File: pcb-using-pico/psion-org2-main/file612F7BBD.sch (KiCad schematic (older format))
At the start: 36 parts, among them SW1 AC_ON, SW10 n, SW11 t, SW12 del, SW13 up, SW14 c, SW15 i, SW16 o, SW17 u, SW18 y, SW19 down, SW2 A, SW20 d, SW21 j, SW22 p, SW23 v, SW24 z, SW25 left, SW26 e, SW27 k, SW28 q, SW29 w, SW3 g, SW30 spc, SW31 right, SW32 f, SW33 L, SW34 r, SW35 x, SW36 exe, SW4 m, SW5 s, SW6 shft, SW7 mode, SW8 b, SW9 h

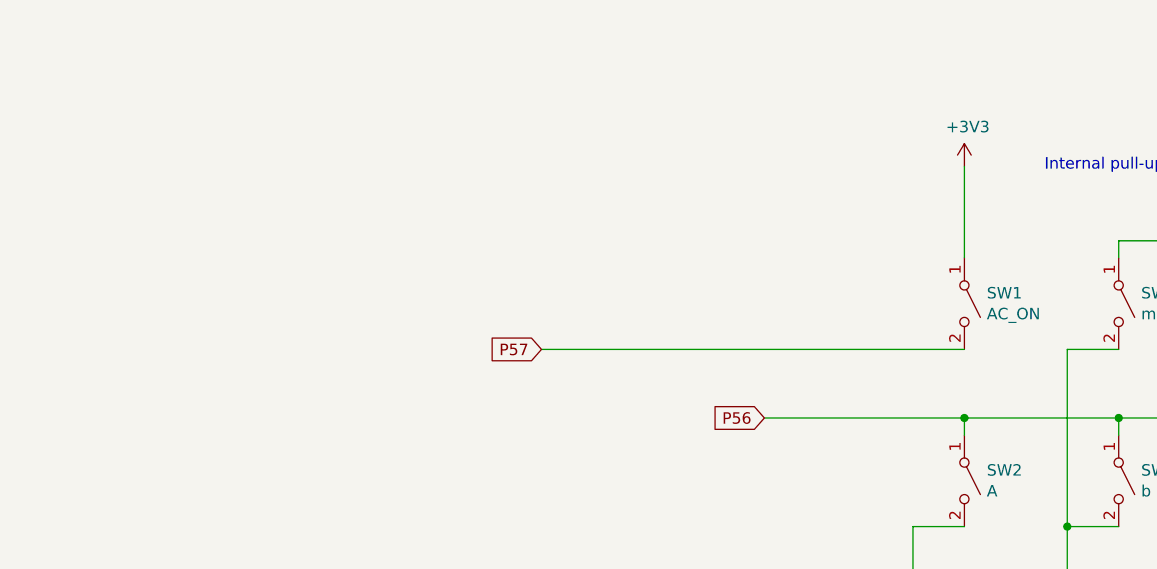
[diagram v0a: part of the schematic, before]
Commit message: Added second connector, eeprom on power pcb
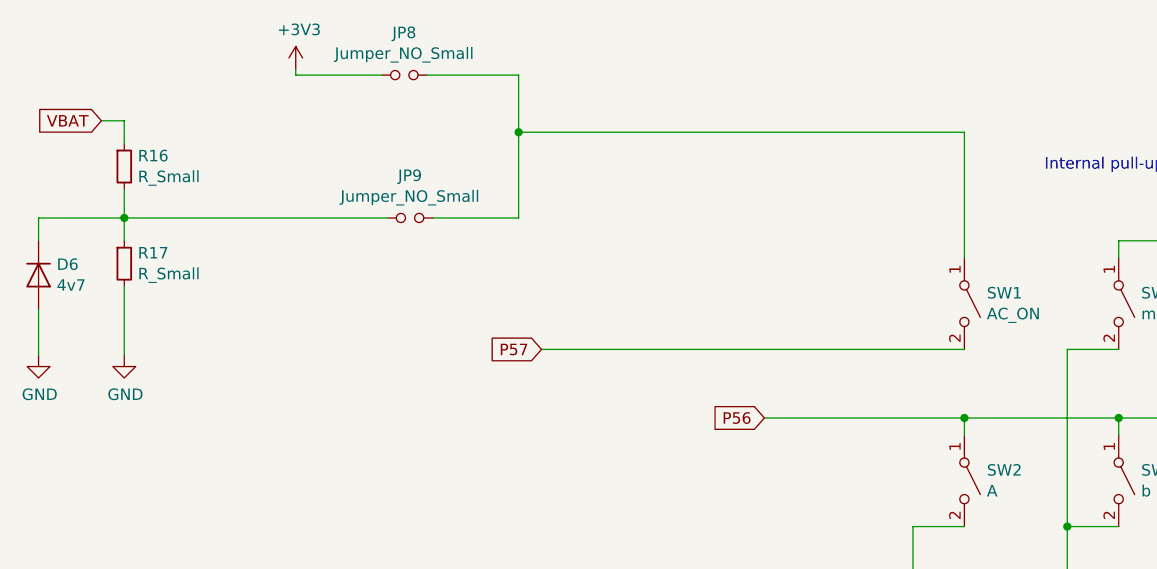
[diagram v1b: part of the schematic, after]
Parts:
- added D6: 4v7, Diode_SMD:D_SOD-123, symbol Device:D
- added JP8, JP9: Jumper_NO_Small, Jumper:SolderJumper-2_P1.3mm_Open_RoundedPad1.0x1.5mm, symbol Device:Jumper_NO_Small
- added R16, R17: R_Small, Resistor_SMD:R_0805_2012Metric, symbol Device:R_Small
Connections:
- net +3V3: now also JP8.1; no longer SW1.1 (A)
- new net: JP8.2, JP9.2, SW1.1 (A)
- new net: D6.1 (K), JP9.1, R16.2, R17.1
- new net GND: D6.2 (A), R17.2
- new net VBAT: R16.1
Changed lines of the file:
@@
 L power:+3V3 #PWR036
 U 1 1 61827F51
-P 6050 1150
-F 0 "#PWR036" H 6050 1000 50  0001 C CNN
-F 1 "+3V3" H 6065 1323 50  0000 C CNN
-F 2 "" H 6050 1150 50  0001 C CNN
-F 3 "" H 6050 1150 50  0001 C CNN
-	1    6050 1150
+P 3125 725
+F 0 "#PWR036" H 3125 575 50  0001 C CNN
+F 1 "+3V3" H 3140 898 50  0000 C CNN
+F 2 "" H 3125 725 50  0001 C CNN
+F 3 "" H 3125 725 50  0001 C CNN
+	1    3125 725
 	1    0    0    -1
 $EndComp
-Wire Wire Line
-	6050 1150 6050 1550
 Text GLabel 9875 950  1    50   Input ~ 0
 K1
@@
 Wire Wire Line
 	5200 5175 6050 5175
+$Comp
+L Device:R_Small R17
+U 1 1 618E7FEC
+P 2375 1575
+F 0 "R17" H 2434 1621 50  0000 L CNN
+F 1 "R_Small" H 2434 1530 50  0000 L CNN
+F 2 "Resistor_SMD:R_0805_2012Metric" H 2375 1575 50  0001 C CNN
+F 3 "~" H 2375 1575 50  0001 C CNN
+	1    2375 1575
+	1    0    0    -1
+$EndComp
+$Comp
+L Device:R_Small R16
+U 1 1 618E840C
+P 2375 1150
+F 0 "R16" H 2434 1196 50  0000 L CNN
+F 1 "R_Small" H 2434 1105 50  0000 L CNN
+F 2 "Resistor_SMD:R_0805_2012Metric" H 2375 1150 50  0001 C CNN
+F 3 "~" H 2375 1150 50  0001 C CNN
+	1    2375 1150
+	1    0    0    -1
+$EndComp
+$Comp
+L Device:D D6
+U 1 1 618E8BE1
+P 2000 1625
+F 0 "D6" V 1954 1704 50  0000 L CNN
+F 1 "4v7" V 2045 1704 50  0000 L CNN
+F 2 "Diode_SMD:D_SOD-123" H 2000 1625 50  0001 C CNN
+F 3 "~" H 2000 1625 50  0001 C CNN
+	1    2000 1625
+	0    1    1    0
+$EndComp
+Wire Wire Line
+	3125 725  3125 750
+Wire Wire Line
+	6050 1000 6050 1550
+Wire Wire Line
+	2375 1050 2375 950
+Wire Wire Line
+	2375 1250 2375 1375
+Wire Wire Line
+	2375 1375 2000 1375
+Wire Wire Line
+	2000 1375 2000 1475
+Connection ~ 2375 1375
+Wire Wire Line
+	2375 1375 2375 1475
+$Comp
+L power:GND #PWR0110
+U 1 1 61919262
+P 2000 1975
+F 0 "#PWR0110" H 2000 1725 50  0001 C CNN
+F 1 "GND" H 2005 1802 50  0000 C CNN
+F 2 "" H 2000 1975 50  0001 C CNN
+F 3 "" H 2000 1975 50  0001 C CNN
+	1    2000 1975
+	1    0    0    -1
+$EndComp
+$Comp
+L power:GND #PWR0111
+U 1 1 619195FD
+P 2375 1975
+F 0 "#PWR0111" H 2375 1725 50  0001 C CNN
+F 1 "GND" H 2380 1802 50  0000 C CNN
+F 2 "" H 2375 1975 50  0001 C CNN
+F 3 "" H 2375 1975 50  0001 C CNN
+	1    2375 1975
+	1    0    0    -1
+$EndComp
+Wire Wire Line
+	2375 1975 2375 1675
+Wire Wire Line
+	2000 1975 2000 1775
+Text GLabel 2275 950  0    50   Input ~ 0
+VBAT
+Wire Wire Line
+	2275 950  2375 950
+$Comp
+L Device:Jumper_NO_Small JP8
+U 1 1 61F117AF
+P 3600 750
+F 0 "JP8" H 3600 935 50  0000 C CNN
+F 1 "Jumper_NO_Small" H 3600 844 50  0000 C CNN
+F 2 "Jumper:SolderJumper-2_P1.3mm_Open_RoundedPad1.0x1.5mm" H 3600 750 50  0001 C CNN
+F 3 "~" H 3600 750 50  0001 C CNN
+	1    3600 750
+	1    0    0    -1
+$EndComp
+$Comp
+L Device:Jumper_NO_Small JP9
+U 1 1 61F123C6
+P 3625 1375
+F 0 "JP9" H 3625 1560 50  0000 C CNN
+F 1 "Jumper_NO_Small" H 3625 1469 50  0000 C CNN
+F 2 "Jumper:SolderJumper-2_P1.3mm_Open_RoundedPad1.0x1.5mm" H 3625 1375 50  0001 C CNN
+F 3 "~" H 3625 1375 50  0001 C CNN
+	1    3625 1375
+	1    0    0    -1
+$EndComp
+Wire Wire Line
+	2375 1375 3525 1375
+Wire Wire Line
+	3125 750  3500 750
+Wire Wire Line
+	3725 1375 4100 1375
+Wire Wire Line
+	4100 1375 4100 1000
+Wire Wire Line
+	4100 750  3700 750
+Wire Wire Line
+	6050 1000 4100 1000
+Connection ~ 4100 1000
+Wire Wire Line
+	4100 1000 4100 750
 $EndSCHEMATC

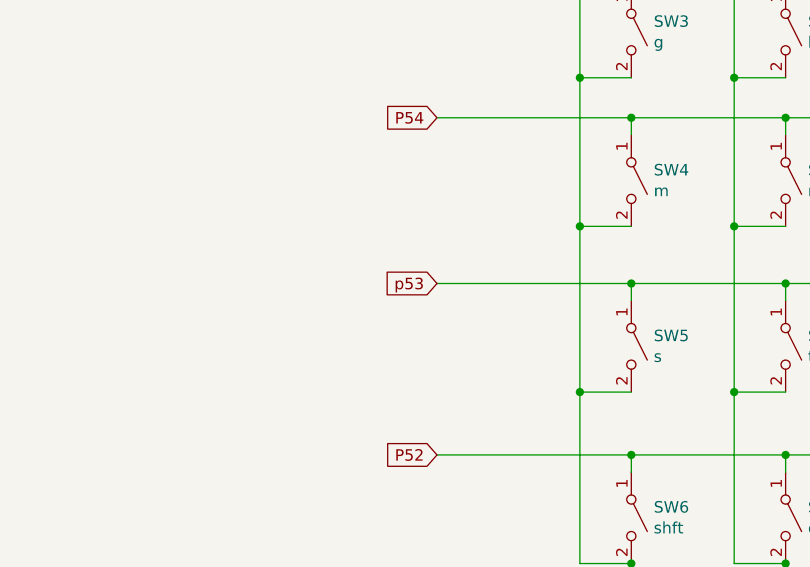
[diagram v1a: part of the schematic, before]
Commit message: Added fab1 archive and small fixes to emulator
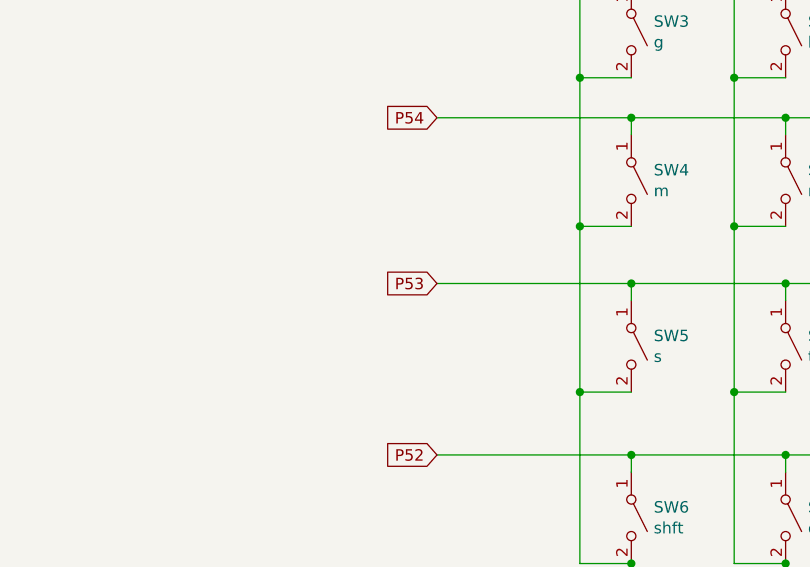
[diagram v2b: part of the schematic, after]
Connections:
- net p53 renamed P53
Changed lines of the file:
@@
 P54
 Text GLabel 5200 4425 0    50   Input ~ 0
-p53
+P53
 Text GLabel 5200 5175 0    50   Input ~ 0
 P52

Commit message: Updates after fab1
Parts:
- D6: value 4v7 -> 2v7
- R16: value R_Small -> 2k2
- R17: value R_Small -> nopop
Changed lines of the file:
@@
 P 2375 1575
 F 0 "R17" H 2434 1621 50  0000 L CNN
-F 1 "R_Small" H 2434 1530 50  0000 L CNN
+F 1 "nopop" H 2434 1530 50  0000 L CNN
 F 2 "Resistor_SMD:R_0805_2012Metric" H 2375 1575 50  0001 C CNN
 F 3 "~" H 2375 1575 50  0001 C CNN
@@
 P 2375 1150
 F 0 "R16" H 2434 1196 50  0000 L CNN
-F 1 "R_Small" H 2434 1105 50  0000 L CNN
+F 1 "2k2" H 2434 1105 50  0000 L CNN
 F 2 "Resistor_SMD:R_0805_2012Metric" H 2375 1150 50  0001 C CNN
 F 3 "~" H 2375 1150 50  0001 C CNN
@@
 P 2000 1625
 F 0 "D6" V 1954 1704 50  0000 L CNN
-F 1 "4v7" V 2045 1704 50  0000 L CNN
+F 1 "2v7" V 2045 1704 50  0000 L CNN
 F 2 "Diode_SMD:D_SOD-123" H 2000 1625 50  0001 C CNN
 F 3 "~" H 2000 1625 50  0001 C CNN

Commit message: V1.1 started
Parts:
- removed JP8, JP9: Jumper_NO_Small, Jumper:SolderJumper-2_P1.3mm_Open_RoundedPad1.0x1.5mm, symbol Device:Jumper_NO_Small
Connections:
- net K3: no longer SW7.2 (B)
- net K4: no longer SW13.2 (B)
- net K5: no longer SW25.2 (B)
- net K6: no longer SW31.2 (B)
- net K7: no longer SW19.2 (B)
- net P52: now also SW7.2 (B)
- net P53: now also SW13.2 (B)
- net P54: now also SW19.2 (B)
- net P55: now also SW25.2 (B)
- net P56: now also SW31.2 (B)
- net P57: now also D6.1 (K), R16.2, R17.1; no longer SW1.2 (B)
- net VBAT: now also SW1.1 (A); no longer R16.1
- new net: R16.1, SW1.2 (B)
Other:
- moved on the sheet: D6, R16, R17
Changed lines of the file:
@@
 encoding utf-8
 Sheet 2 2
-Title ""
-Date ""
-Rev ""
-Comp ""
+Title "Psion Organiser II Re-Creation"
+Date "2021-12-27"
+Rev "V1.1"
+Comp "A Menadue"
 Comment1 ""
 Comment2 ""
@@
 Connection ~ 5825 4900
 Wire Wire Line
-	6500 1950 6725 1950
-Wire Wire Line
-	6500 1950 6500 2725
-Wire Wire Line
 	6500 2725 6725 2725
 Wire Wire Line
@@
 Wire Wire Line
 	6500 3525 6725 3525
-Connection ~ 6500 2725
 Wire Wire Line
 	6500 3525 6500 4175
@@
 Connection ~ 6500 4900
 Wire Wire Line
-	7175 1950 7400 1950
-Wire Wire Line
-	7175 1950 7175 2725
-Wire Wire Line
 	7175 2725 7400 2725
 Wire Wire Line
@@
 Wire Wire Line
 	7175 3525 7400 3525
-Connection ~ 7175 2725
 Wire Wire Line
 	7175 3525 7175 4175
@@
 Connection ~ 7175 4900
 Wire Wire Line
-	7825 1950 8050 1950
-Wire Wire Line
-	7825 1950 7825 2725
-Wire Wire Line
 	7825 2725 8050 2725
 Wire Wire Line
@@
 Wire Wire Line
 	7825 3525 8050 3525
-Connection ~ 7825 2725
 Wire Wire Line
 	7825 3525 7825 4175
@@
 Connection ~ 7825 4900
 Wire Wire Line
-	8450 1975 8675 1975
-Wire Wire Line
-	8450 1975 8450 2750
-Wire Wire Line
 	8450 2750 8675 2750
 Wire Wire Line
@@
 Wire Wire Line
 	8450 3550 8675 3550
-Connection ~ 8450 2750
 Wire Wire Line
 	8450 3550 8450 4200
@@
 Connection ~ 8450 4925
 Wire Wire Line
-	9050 1975 9275 1975
-Wire Wire Line
-	9050 1975 9050 2750
-Wire Wire Line
 	9050 2750 9275 2750
 Wire Wire Line
@@
 Wire Wire Line
 	9050 3550 9275 3550
-Connection ~ 9050 2750
 Wire Wire Line
 	9050 3550 9050 4200
@@
 	9275 2350 9275 2250
 Wire Wire Line
-	9275 2250 8675 2250
+	9275 2250 8975 2250
 Wire Wire Line
 	8675 2250 8675 2350
@@
 	8675 3050 8675 3150
 Wire Wire Line
-	8675 3050 8050 3050
+	8675 3050 8350 3050
 Wire Wire Line
 	8050 3050 8050 3125
@@
 Connection ~ 8675 3700
 Wire Wire Line
-	8050 3700 7400 3700
+	8050 3700 7750 3700
 Wire Wire Line
 	7400 3700 7400 3775
@@
 Connection ~ 8050 4425
 Wire Wire Line
-	7400 4425 6725 4425
+	7400 4425 7075 4425
 Wire Wire Line
 	6725 4425 6725 4500
@@
 Connection ~ 7400 5175
 Wire Wire Line
-	6725 5175 6050 5175
+	6725 5175 6375 5175
 Wire Wire Line
 	6050 5175 6050 5250
@@
 	6050 5800 6050 5650
 Connection ~ 6050 5650
-Text GLabel 4200 1950 0    50   Input ~ 0
+Text GLabel 2075 2625 0    50   Input ~ 0
 P57
-$Comp
-L power:+3V3 #PWR036
-U 1 1 61827F51
-P 3125 725
-F 0 "#PWR036" H 3125 575 50  0001 C CNN
-F 1 "+3V3" H 3140 898 50  0000 C CNN
-F 2 "" H 3125 725 50  0001 C CNN
-F 3 "" H 3125 725 50  0001 C CNN
-	1    3125 725
-	1    0    0    -1
-$EndComp
 Text GLabel 9875 950  1    50   Input ~ 0
 K1
@@
 Connection ~ 7400 1475
 Wire Wire Line
-	4200 1950 6050 1950
-Wire Wire Line
 	5175 2250 6050 2250
 Wire Wire Line
@@
 L Device:R_Small R17
 U 1 1 618E7FEC
-P 2375 1575
-F 0 "R17" H 2434 1621 50  0000 L CNN
-F 1 "nopop" H 2434 1530 50  0000 L CNN
-F 2 "Resistor_SMD:R_0805_2012Metric" H 2375 1575 50  0001 C CNN
-F 3 "~" H 2375 1575 50  0001 C CNN
-	1    2375 1575
+P 2625 2825
+F 0 "R17" H 2684 2871 50  0000 L CNN
+F 1 "nopop" H 2684 2780 50  0000 L CNN
+F 2 "Resistor_SMD:R_0805_2012Metric" H 2625 2825 50  0001 C CNN
+F 3 "~" H 2625 2825 50  0001 C CNN
+	1    2625 2825
 	1    0    0    -1
 $EndComp
@@
 L Device:R_Small R16
 U 1 1 618E840C
-P 2375 1150
-F 0 "R16" H 2434 1196 50  0000 L CNN
-F 1 "2k2" H 2434 1105 50  0000 L CNN
-F 2 "Resistor_SMD:R_0805_2012Metric" H 2375 1150 50  0001 C CNN
-F 3 "~" H 2375 1150 50  0001 C CNN
-	1    2375 1150
+P 2625 2400
+F 0 "R16" H 2684 2446 50  0000 L CNN
+F 1 "2k2" H 2684 2355 50  0000 L CNN
+F 2 "Resistor_SMD:R_0805_2012Metric" H 2625 2400 50  0001 C CNN
+F 3 "~" H 2625 2400 50  0001 C CNN
+	1    2625 2400
 	1    0    0    -1
 $EndComp
@@
 L Device:D D6
 U 1 1 618E8BE1
-P 2000 1625
-F 0 "D6" V 1954 1704 50  0000 L CNN
-F 1 "2v7" V 2045 1704 50  0000 L CNN
-F 2 "Diode_SMD:D_SOD-123" H 2000 1625 50  0001 C CNN
-F 3 "~" H 2000 1625 50  0001 C CNN
-	1    2000 1625
-	0    1    1    0
-$EndComp
-Wire Wire Line
-	3125 725  3125 750
-Wire Wire Line
-	6050 1000 6050 1550
-Wire Wire Line
-	2375 1050 2375 950
-Wire Wire Line
-	2375 1250 2375 1375
-Wire Wire Line
-	2375 1375 2000 1375
-Wire Wire Line
-	2000 1375 2000 1475
-Connection ~ 2375 1375
-Wire Wire Line
-	2375 1375 2375 1475
+P 2250 2875
+F 0 "D6" V 2204 2954 50  0000 L CNN
+F 1 "2v7" V 2295 2954 50  0000 L CNN
+F 2 "Diode_SMD:D_SOD-123" H 2250 2875 50  0001 C CNN
+F 3 "~" H 2250 2875 50  0001 C CNN
+	1    2250 2875
+	0    1    1    0
+$EndComp
+Wire Wire Line
+	2625 2500 2625 2625
+Wire Wire Line
+	2625 2625 2250 2625
+Wire Wire Line
+	2250 2625 2250 2725
+Connection ~ 2625 2625
+Wire Wire Line
+	2625 2625 2625 2725
 $Comp
 L power:GND #PWR0110
 U 1 1 61919262
-P 2000 1975
-F 0 "#PWR0110" H 2000 1725 50  0001 C CNN
-F 1 "GND" H 2005 1802 50  0000 C CNN
-F 2 "" H 2000 1975 50  0001 C CNN
-F 3 "" H 2000 1975 50  0001 C CNN
-	1    2000 1975
+P 2250 3225
+F 0 "#PWR0110" H 2250 2975 50  0001 C CNN
+F 1 "GND" H 2255 3052 50  0000 C CNN
+F 2 "" H 2250 3225 50  0001 C CNN
+F 3 "" H 2250 3225 50  0001 C CNN
+	1    2250 3225
 	1    0    0    -1
 $EndComp
@@
 L power:GND #PWR0111
 U 1 1 619195FD
-P 2375 1975
-F 0 "#PWR0111" H 2375 1725 50  0001 C CNN
-F 1 "GND" H 2380 1802 50  0000 C CNN
-F 2 "" H 2375 1975 50  0001 C CNN
-F 3 "" H 2375 1975 50  0001 C CNN
-	1    2375 1975
+P 2625 3225
+F 0 "#PWR0111" H 2625 2975 50  0001 C CNN
+F 1 "GND" H 2630 3052 50  0000 C CNN
+F 2 "" H 2625 3225 50  0001 C CNN
+F 3 "" H 2625 3225 50  0001 C CNN
+	1    2625 3225
 	1    0    0    -1
 $EndComp
 Wire Wire Line
-	2375 1975 2375 1675
-Wire Wire Line
-	2000 1975 2000 1775
-Text GLabel 2275 950  0    50   Input ~ 0
+	2625 3225 2625 2925
+Wire Wire Line
+	2250 3225 2250 3025
+Text GLabel 5200 1200 0    50   Input ~ 0
 VBAT
 Wire Wire Line
-	2275 950  2375 950
-$Comp
-L Device:Jumper_NO_Small JP8
-U 1 1 61F117AF
-P 3600 750
-F 0 "JP8" H 3600 935 50  0000 C CNN
-F 1 "Jumper_NO_Small" H 3600 844 50  0000 C CNN
-F 2 "Jumper:SolderJumper-2_P1.3mm_Open_RoundedPad1.0x1.5mm" H 3600 750 50  0001 C CNN
-F 3 "~" H 3600 750 50  0001 C CNN
-	1    3600 750
-	1    0    0    -1
-$EndComp
-$Comp
-L Device:Jumper_NO_Small JP9
-U 1 1 61F123C6
-P 3625 1375
-F 0 "JP9" H 3625 1560 50  0000 C CNN
-F 1 "Jumper_NO_Small" H 3625 1469 50  0000 C CNN
-F 2 "Jumper:SolderJumper-2_P1.3mm_Open_RoundedPad1.0x1.5mm" H 3625 1375 50  0001 C CNN
-F 3 "~" H 3625 1375 50  0001 C CNN
-	1    3625 1375
-	1    0    0    -1
-$EndComp
-Wire Wire Line
-	2375 1375 3525 1375
-Wire Wire Line
-	3125 750  3500 750
-Wire Wire Line
-	3725 1375 4100 1375
-Wire Wire Line
-	4100 1375 4100 1000
-Wire Wire Line
-	4100 750  3700 750
-Wire Wire Line
-	6050 1000 4100 1000
-Connection ~ 4100 1000
-Wire Wire Line
-	4100 1000 4100 750
+	5200 1200 6050 1200
+Wire Wire Line
+	6050 1200 6050 1550
+Wire Wire Line
+	2075 2625 2250 2625
+Connection ~ 2250 2625
+Wire Wire Line
+	2625 2300 2625 1950
+Wire Wire Line
+	2625 1950 6050 1950
+Wire Wire Line
+	6375 1950 6375 5175
+Wire Wire Line
+	6375 1950 6725 1950
+Connection ~ 6375 5175
+Wire Wire Line
+	6375 5175 6050 5175
+Wire Wire Line
+	7075 1950 7075 4425
+Wire Wire Line
+	7075 1950 7400 1950
+Connection ~ 7075 4425
+Wire Wire Line
+	7075 4425 6725 4425
+Wire Wire Line
+	7750 1950 7750 3700
+Wire Wire Line
+	7750 1950 8050 1950
+Connection ~ 7750 3700
+Wire Wire Line
+	7750 3700 7400 3700
+Wire Wire Line
+	8350 1975 8350 3050
+Wire Wire Line
+	8350 1975 8675 1975
+Connection ~ 8350 3050
+Wire Wire Line
+	8350 3050 8050 3050
+Wire Wire Line
+	8975 1975 8975 2250
+Wire Wire Line
+	8975 1975 9275 1975
+Connection ~ 8975 2250
+Wire Wire Line
+	8975 2250 8675 2250
 $EndSCHEMATC
